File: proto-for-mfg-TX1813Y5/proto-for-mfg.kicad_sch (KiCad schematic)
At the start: 57 parts, among them J1 Conn_01x03_Pin

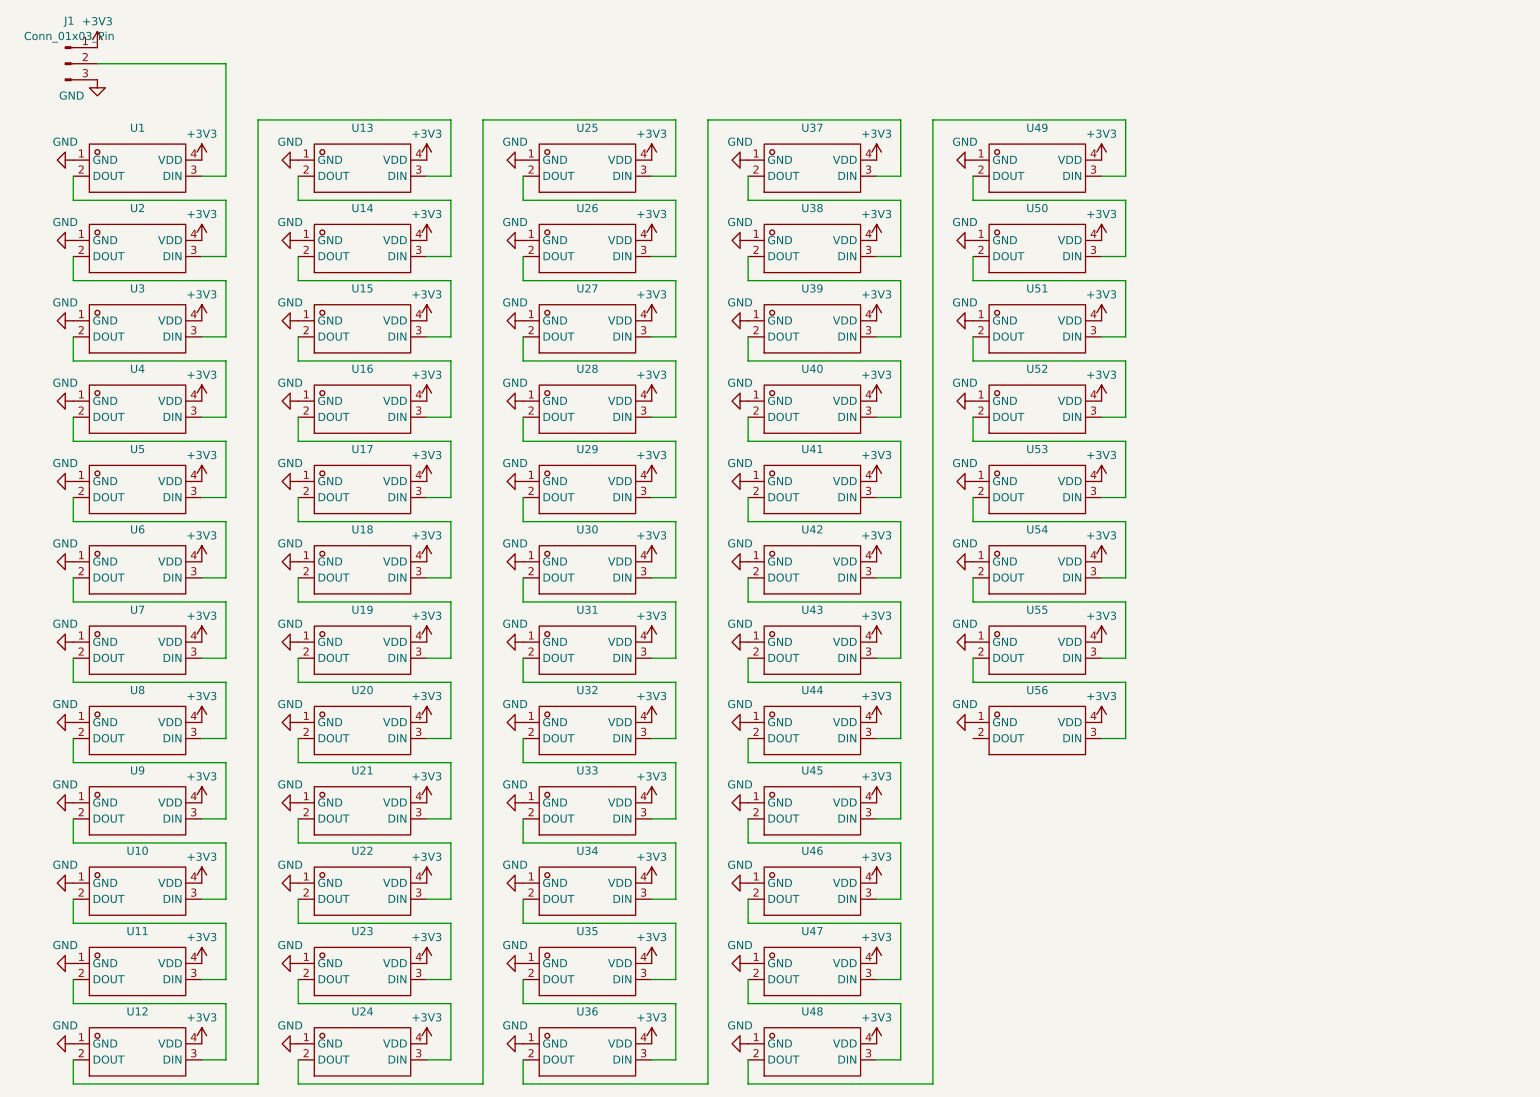
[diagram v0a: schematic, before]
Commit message: move over to new LED and fix design
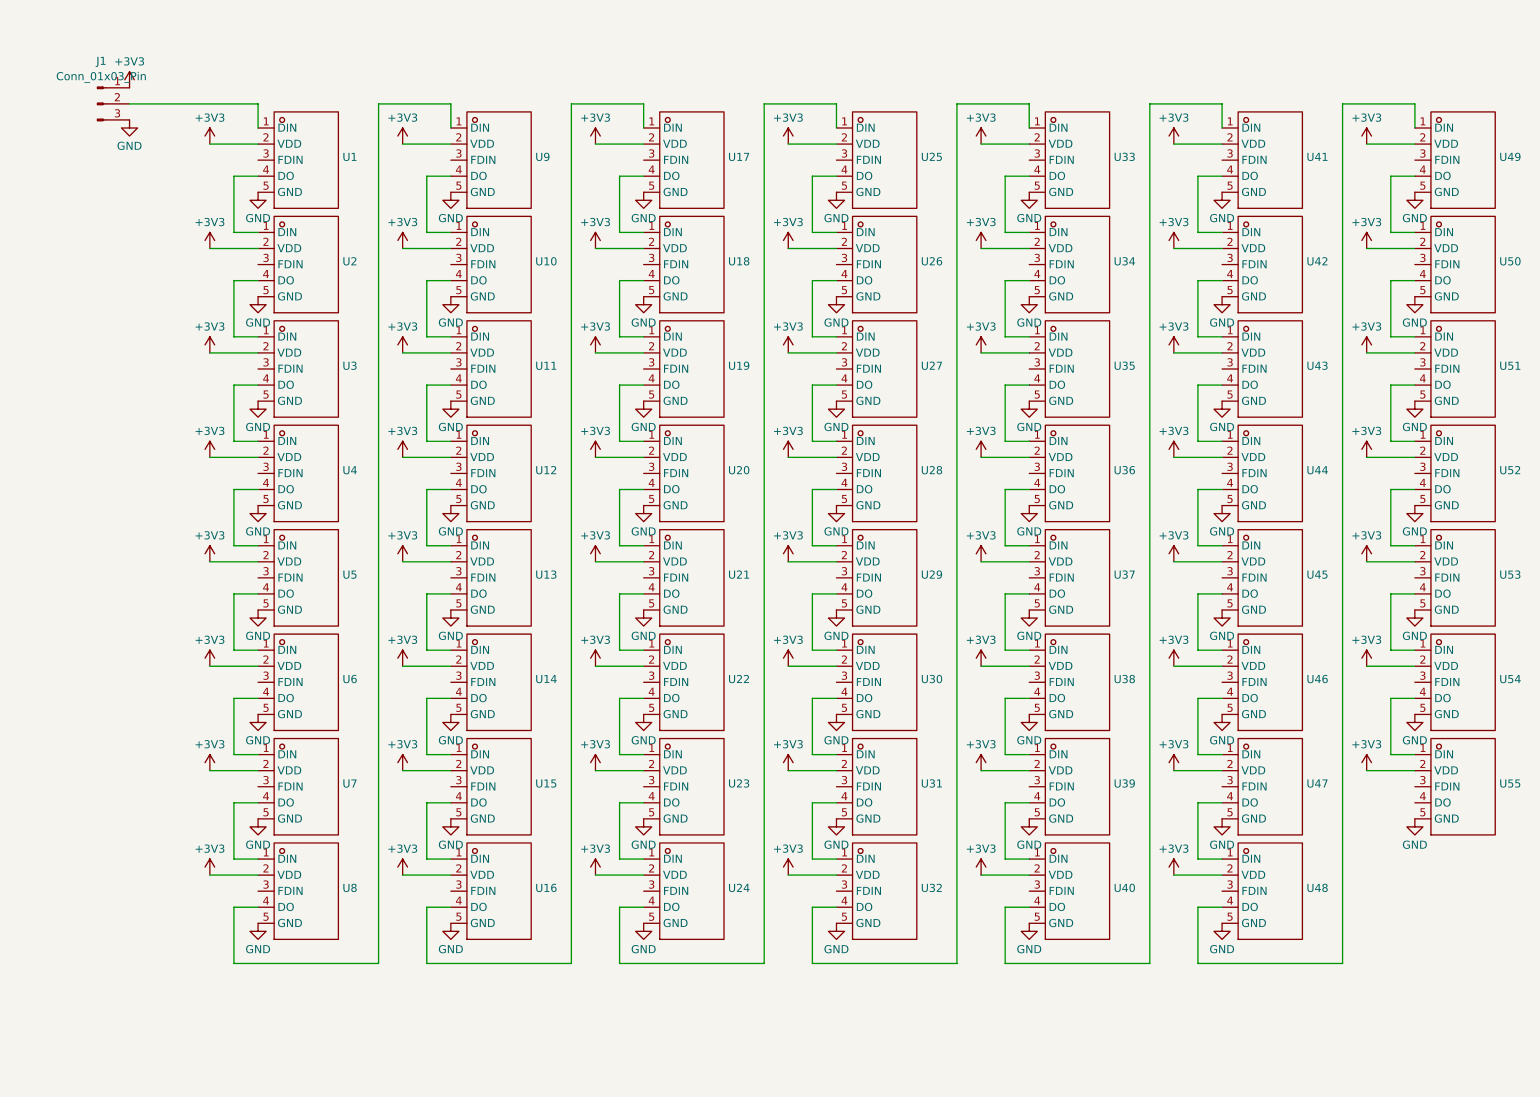
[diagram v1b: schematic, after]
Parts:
- removed U10, U11, U12, U13, U14, U15, U16, U17, U18, U19, U2, U20, U21, U22, U23, U24, U25, U26, U27, U28, U29, U3, U30, U31, U32, U33, U34, U35, U36, U37, U38, U39, U4, U40, U41, U42, U43, U44, U45, U46, U47, U48, U49, U5, U50, U51, U52, U53, U54, U55, U56, U6, U7, U8, U9: ~, ProLib_pcs_2025-03-31:LED-SMD_4P_SK6812D-EC3210R, symbol LED:SK6812D-EC3210R
- added U10, U11, U12, U13, U14, U15, U16, U17, U18, U19, U2, U20, U21, U22, U23, U24, U25, U26, U27, U28, U29, U3, U30, U31, U32, U33, U34, U35, U36, U37, U38, U39, U4, U40, U41, U42, U43, U44, U45, U46, U47, U48, U49, U5, U50, U51, U52, U53, U54, U55, U6, U7, U8, U9: ~, LED_SMD:LED-SMD_5P-L3.2-W1.4_TX1813Y5, symbol LED:TX1813Y5
- U1: footprint ProLib_pcs_2025-03-31:LED-SMD_4P_SK6812D-EC3210R -> LED_SMD:LED-SMD_5P-L3.2-W1.4_TX1813Y5; symbol LED:SK6812D-EC3210R -> LED:TX1813Y5; LCSC Part Name RGB三色 -> TX1813Y5; Manufacturer 欧思科光电 -> TCWIN(天成); Manufacturer Part SK6812D-EC3210R -> TX1813Y5; Supplier Part C2890041 -> C3975084
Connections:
- net +3V3: now also U1.2 (VDD), U10.2 (VDD), U11.2 (VDD), U12.2 (VDD), U13.2 (VDD), U14.2 (VDD), U15.2 (VDD), U16.2 (VDD), U17.2 (VDD), U18.2 (VDD), U19.2 (VDD), U2.2 (VDD), U20.2 (VDD), U21.2 (VDD), U22.2 (VDD), U23.2 (VDD), U24.2 (VDD), U25.2 (VDD), U26.2 (VDD), U27.2 (VDD), U28.2 (VDD), U29.2 (VDD), U3.2 (VDD), U30.2 (VDD), U31.2 (VDD), U32.2 (VDD), U33.2 (VDD), U34.2 (VDD), U35.2 (VDD), U36.2 (VDD), U37.2 (VDD), U38.2 (VDD), U39.2 (VDD), U4.2 (VDD), U40.2 (VDD), U41.2 (VDD), U42.2 (VDD), U43.2 (VDD), U44.2 (VDD), U45.2 (VDD), U46.2 (VDD), U47.2 (VDD), U48.2 (VDD), U49.2 (VDD), U5.2 (VDD), U50.2 (VDD), U51.2 (VDD), U52.2 (VDD), U53.2 (VDD), U54.2 (VDD), U55.2 (VDD), U6.2 (VDD), U7.2 (VDD), U8.2 (VDD), U9.2 (VDD); no longer U1.4 (VDD)
- net GND: now also U1.5 (GND), U10.5 (GND), U11.5 (GND), U12.5 (GND), U13.5 (GND), U14.5 (GND), U15.5 (GND), U16.5 (GND), U17.5 (GND), U18.5 (GND), U19.5 (GND), U2.5 (GND), U20.5 (GND), U21.5 (GND), U22.5 (GND), U23.5 (GND), U24.5 (GND), U25.5 (GND), U26.5 (GND), U27.5 (GND), U28.5 (GND), U29.5 (GND), U3.5 (GND), U30.5 (GND), U31.5 (GND), U32.5 (GND), U33.5 (GND), U34.5 (GND), U35.5 (GND), U36.5 (GND), U37.5 (GND), U38.5 (GND), U39.5 (GND), U4.5 (GND), U40.5 (GND), U41.5 (GND), U42.5 (GND), U43.5 (GND), U44.5 (GND), U45.5 (GND), U46.5 (GND), U47.5 (GND), U48.5 (GND), U49.5 (GND), U5.5 (GND), U50.5 (GND), U51.5 (GND), U52.5 (GND), U53.5 (GND), U54.5 (GND), U55.5 (GND), U6.5 (GND), U7.5 (GND), U8.5 (GND), U9.5 (GND); no longer U1.1 (GND)
- net at J1.2 (Pin_2): now also U1.1 (DIN); no longer U1.3 (DIN)
- new net: U51.4 (DO), U52.1 (DIN)
- new net: U52.4 (DO), U53.1 (DIN)
- new net: U14.4 (DO), U15.1 (DIN)
- new net: U15.4 (DO), U16.1 (DIN)
- new net: U45.4 (DO), U46.1 (DIN)
- new net: U46.4 (DO), U47.1 (DIN)
- new net: U2.4 (DO), U3.1 (DIN)
- new net: U3.4 (DO), U4.1 (DIN)
- new net: U4.4 (DO), U5.1 (DIN)
- new net: U5.4 (DO), U6.1 (DIN)
- new net: U47.4 (DO), U48.1 (DIN)
- new net: U12.4 (DO), U13.1 (DIN)
- new net: U13.4 (DO), U14.1 (DIN)
- new net: U21.4 (DO), U22.1 (DIN)
- new net: U22.4 (DO), U23.1 (DIN)
- new net: U16.4 (DO), U17.1 (DIN)
- new net: U32.4 (DO), U33.1 (DIN)
- new net: U33.4 (DO), U34.1 (DIN)
- new net: U48.4 (DO), U49.1 (DIN)
- new net: U49.4 (DO), U50.1 (DIN)
- new net: U1.4 (DO), U2.1 (DIN)
- new net: U10.4 (DO), U11.1 (DIN)
- new net: U11.4 (DO), U12.1 (DIN)
- new net: U40.4 (DO), U41.1 (DIN)
- new net: U41.4 (DO), U42.1 (DIN)
- new net: U54.4 (DO), U55.1 (DIN)
- new net: U29.4 (DO), U30.1 (DIN)
- new net: U30.4 (DO), U31.1 (DIN)
- new net: U42.4 (DO), U43.1 (DIN)
- new net: U43.4 (DO), U44.1 (DIN)
- new net: U35.4 (DO), U36.1 (DIN)
- new net: U36.4 (DO), U37.1 (DIN)
- new net: U44.4 (DO), U45.1 (DIN)
- new net: U23.4 (DO), U24.1 (DIN)
- new net: U24.4 (DO), U25.1 (DIN)
- new net: U37.4 (DO), U38.1 (DIN)
- new net: U38.4 (DO), U39.1 (DIN)
- new net: U34.4 (DO), U35.1 (DIN)
- new net: U31.4 (DO), U32.1 (DIN)
- new net: U26.4 (DO), U27.1 (DIN)
- new net: U27.4 (DO), U28.1 (DIN)
- new net: U6.4 (DO), U7.1 (DIN)
- new net: U17.4 (DO), U18.1 (DIN)
- new net: U18.4 (DO), U19.1 (DIN)
- new net: U39.4 (DO), U40.1 (DIN)
- new net: U53.4 (DO), U54.1 (DIN)
- new net: U28.4 (DO), U29.1 (DIN)
- new net: U20.4 (DO), U21.1 (DIN)
- new net: U7.4 (DO), U8.1 (DIN)
- new net: U25.4 (DO), U26.1 (DIN)
- new net: U50.4 (DO), U51.1 (DIN)
- new net: U8.4 (DO), U9.1 (DIN)
- new net: U10.1 (DIN), U9.4 (DO)
- new net: U19.4 (DO), U20.1 (DIN)
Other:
- moved on the sheet: J1
